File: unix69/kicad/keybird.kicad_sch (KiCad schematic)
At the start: 139 parts, among them J0 Conn_01x23, SW00 SW_Push, SW01 SW_Push, SW02 SW_Push, SW03 SW_Push, SW04 SW_Push, SW05 SW_Push, SW06 SW_Push, SW07 SW_Push, SW10 SW_Push, SW11 SW_Push, SW12 SW_Push, SW13 SW_Push, SW14 SW_Push, SW15 SW_Push, SW16 SW_Push, SW17 SW_Push, SW20 SW_Push, SW21 SW_Push, SW22 SW_Push, SW23 SW_Push, SW24 SW_Push, SW25 SW_Push, SW26 SW_Push, SW27 SW_Push, SW30 SW_Push, SW31 SW_Push, SW32 SW_Push, SW33 SW_Push, SW34 SW_Push, SW35 SW_Push, SW36 SW_Push, SW40 SW_Push, SW41 SW_Push, SW42 SW_Push, SW43 SW_Push, SW44 SW_Push, SW45 SW_Push, SW47 SW_Push, SW50 SW_Push, SW51 SW_Push, SW52 SW_Push, SW53 SW_Push, SW54 SW_Push, SW55 SW_Push, SW56 SW_Push, SW57 SW_Push, SW60 SW_Push, SW61 SW_Push, SW62 SW_Push, SW63 SW_Push, SW64 SW_Push, SW65 SW_Push, SW66 SW_Push, SW67 SW_Push, SW70 SW_Push, SW71 SW_Push, SW72 SW_Push, SW73 SW_Push, SW74 SW_Push, SW75 SW_Push, SW76 SW_Push, SW77 SW_Push, SW80 SW_Push, SW81 SW_Push, SW83 SW_Push, SW84 SW_Push, SW85 SW_Push, SW86 SW_Push, SW87 SW_Push

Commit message: preen annotations and centre rp2040
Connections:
- no-connect marks 80 -> 76
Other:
- note added: "columns on bottom of board"
- note added: "rows on top of board"
- note added: "to Waveshare RP2040-Tiny"
- note removed: "COLUMNS ON BOTTOM OF BOARD"
- note removed: "ROWS ON TOP OF BOARD"
- note removed: "TO GP0"
- note removed: "TO GP1"
- note removed: "TO GP10"
- note removed: "TO GP11"
- note removed: "TO GP12"
- note removed: "TO GP13"
- note removed: "TO GP2"
- note removed: "TO GP26"
- note removed: "TO GP27"
- note removed: "TO GP28"
- note removed: "TO GP29"
- note removed: "TO GP3"
- note removed: "TO GP4"
- note removed: "TO GP5"
- note removed: "TO GP6"
- note removed: "TO GP7"
- note removed: "TO GP8"
- moved on the sheet: J0

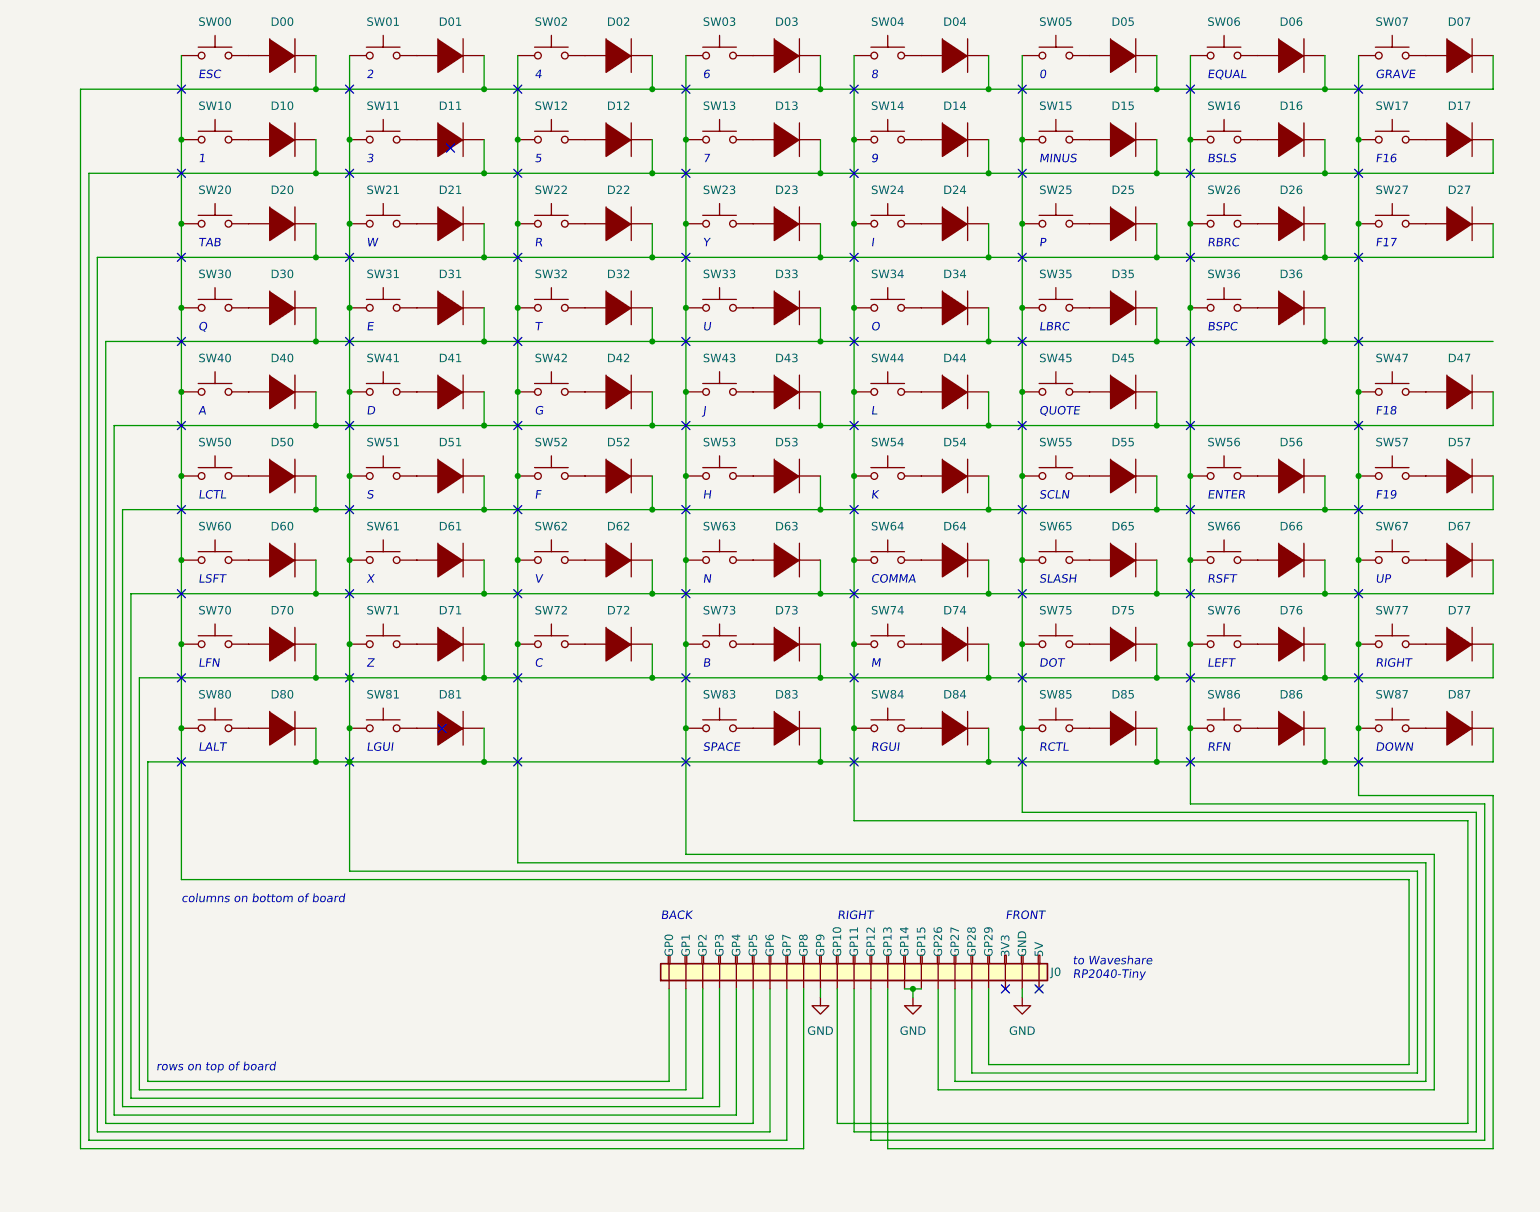
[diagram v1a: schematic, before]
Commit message: use net labels instead of long wires
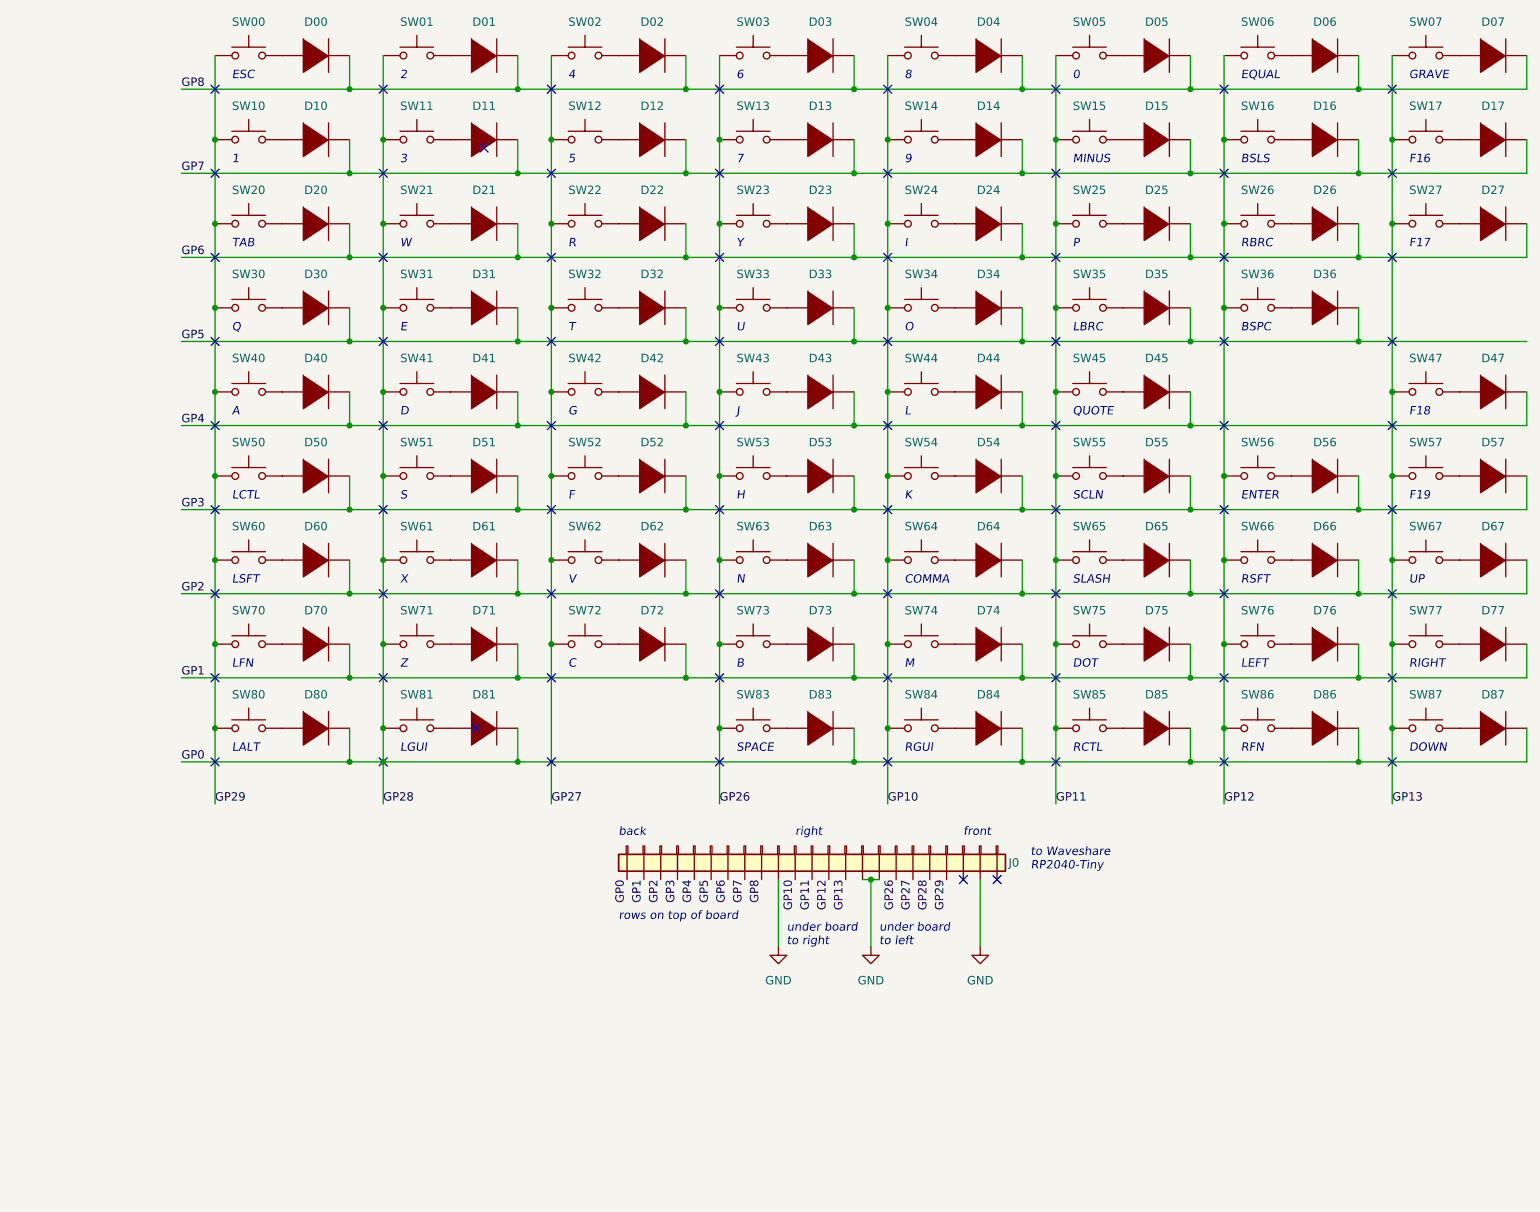
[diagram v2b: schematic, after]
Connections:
- net GP0: now reaches D80.2 (A), D81.2 (A), D83.2 (A), D84.2 (A), D85.2 (A), D86.2 (A), D87.2 (A), J0.1 (GP0), J0.19 (GP28), SW01.1, SW11.1, SW21.1, SW31.1, SW41.1, SW51.1, SW61.1, SW71.1, SW81.1
- net GP0: no longer D70.2 (A), D71.2 (A), D72.2 (A), D73.2 (A), D74.2 (A), D75.2 (A), D76.2 (A), D77.2 (A), J0.2 (GP1)
- net GP10: now reaches J0.11 (GP10), SW04.1, SW14.1, SW24.1, SW34.1, SW44.1, SW54.1, SW64.1, SW74.1, SW84.1
- net GP3: now reaches D50.2 (A), D51.2 (A), D52.2 (A), D53.2 (A), D54.2 (A), D55.2 (A), D56.2 (A), D57.2 (A), J0.4 (GP3)
- net GP2: now reaches D60.2 (A), D61.2 (A), D62.2 (A), D63.2 (A), D64.2 (A), D65.2 (A), D66.2 (A), D67.2 (A), J0.3 (GP2)
- net GP12: now reaches J0.13 (GP12), SW06.1, SW16.1, SW26.1, SW36.1, SW56.1, SW66.1, SW76.1, SW86.1
- net GP26: now reaches J0.17 (GP26), SW03.1, SW13.1, SW23.1, SW33.1, SW43.1, SW53.1, SW63.1, SW73.1, SW83.1
- net GP4: now reaches D40.2 (A), D41.2 (A), D42.2 (A), D43.2 (A), D44.2 (A), D45.2 (A), D47.2 (A), J0.5 (GP4)
- net GP29: now reaches J0.20 (GP29), SW00.1, SW10.1, SW20.1, SW30.1, SW40.1, SW50.1, SW60.1, SW70.1, SW80.1
- net GP27: now reaches J0.18 (GP27), SW02.1, SW12.1, SW22.1, SW32.1, SW42.1, SW52.1, SW62.1, SW72.1
- net GP13: now reaches J0.14 (GP13), SW07.1, SW17.1, SW27.1, SW47.1, SW57.1, SW67.1, SW77.1, SW87.1
- net GP5: now reaches D30.2 (A), D31.2 (A), D32.2 (A), D33.2 (A), D34.2 (A), D35.2 (A), D36.2 (A), J0.6 (GP5)
- net GP11: now reaches J0.12 (GP11), SW05.1, SW15.1, SW25.1, SW35.1, SW45.1, SW55.1, SW65.1, SW75.1, SW85.1
- net GP6: now reaches D20.2 (A), D21.2 (A), D22.2 (A), D23.2 (A), D24.2 (A), D25.2 (A), D26.2 (A), D27.2 (A), J0.7 (GP6)
- net GP8: now reaches D00.2 (A), D01.2 (A), D02.2 (A), D03.2 (A), D04.2 (A), D05.2 (A), D06.2 (A), D07.2 (A), J0.9 (GP8)
- net GP7: now reaches D10.2 (A), D11.2 (A), D12.2 (A), D13.2 (A), D14.2 (A), D15.2 (A), D16.2 (A), D17.2 (A), J0.8 (GP7)
- new net GP1: D70.2 (A), D71.2 (A), D72.2 (A), D73.2 (A), D74.2 (A), D75.2 (A), D76.2 (A), D77.2 (A), J0.2 (GP1)
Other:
- note added: "back"
- note added: "front"
- note added: "right"
- note added: "under board to left"
- note added: "under board to right"
- note removed: "BACK"
- note removed: "FRONT"
- note removed: "columns on bottom of board"
- moved on the sheet: D00, D01, D02, D03, D04, D05, D06, D07, D10, D11, D12, D13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

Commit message: use a proper symbol for the RP20540
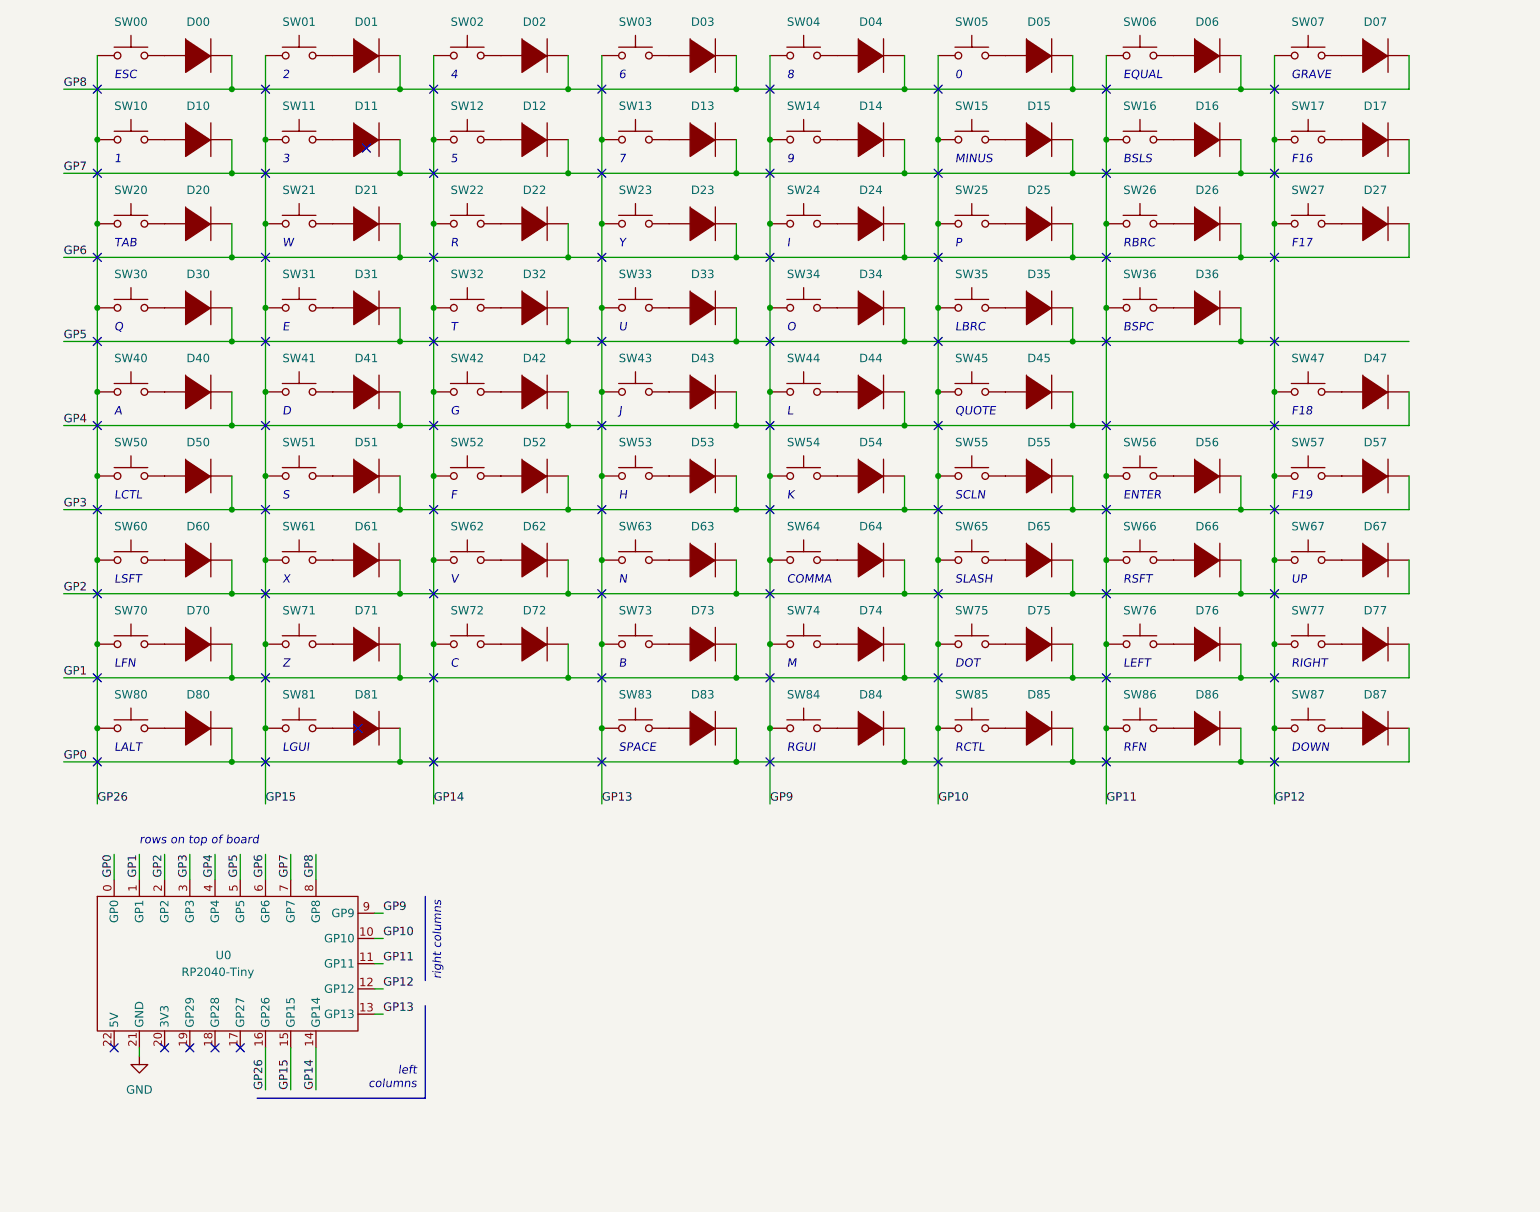
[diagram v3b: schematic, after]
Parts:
- removed J0: Conn_01x23, symbol Connector_Generic:Conn_01x23
- added U0: RP2040-Tiny, Module:RP2040-Tiny, symbol MCU_Module:RP2040-Tiny
- SW00, SW01, SW02, SW03, SW04, SW05, SW06, SW07, SW10, SW11, SW12, SW13, SW14, SW15, SW16, SW17, SW20, SW21, SW22, SW23, SW24, SW25, SW26, SW27, SW30, SW31, SW32, SW33, SW34, SW35, SW36, SW40, SW41, SW42, SW43, SW44, SW45, SW47, SW50, SW51, SW52, SW53, SW54, SW55, SW56, SW57, SW60, SW61, SW62, SW63, SW64, SW65, SW66, SW67, SW70, SW71, SW72, SW73, SW74, SW75, SW76, SW77, SW80, SW81, SW83, SW84, SW85, SW86, SW87: footprint SW_Cherry_MX_1.00u_PCB -> Button_Switch_Keyboard:SW_Cherry_MX_1.00u_PCB
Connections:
- net GP29 is gone; now on net GP26: SW00.1, SW10.1, SW20.1, SW30.1, SW40.1, SW50.1, SW60.1, SW70.1, SW80.1
- net GND: now also U0.21 (GND)
- net GP0: now also U0.0 (GP0); no longer SW01.1, SW11.1, SW21.1, SW31.1, SW41.1, SW51.1, SW61.1, SW71.1, SW81.1
- net GP1: now also U0.1 (GP1)
- net GP10: now also SW05.1, SW15.1, SW25.1, SW35.1, SW45.1, SW55.1, SW65.1, SW75.1, SW85.1, U0.10 (GP10); no longer SW04.1, SW14.1, SW24.1, SW34.1, SW44.1, SW54.1, SW64.1, SW74.1, SW84.1
- net GP11: now also SW06.1, SW16.1, SW26.1, SW36.1, SW56.1, SW66.1, SW76.1, SW86.1, U0.11 (GP11); no longer SW05.1, SW15.1, SW25.1, SW35.1, SW45.1, SW55.1, SW65.1, SW75.1, SW85.1
- net GP12: now also SW07.1, SW17.1, SW27.1, SW47.1, SW57.1, SW67.1, SW77.1, SW87.1, U0.12 (GP12); no longer SW06.1, SW16.1, SW26.1, SW36.1, SW56.1, SW66.1, SW76.1, SW86.1
- net GP13: now also SW03.1, SW13.1, SW23.1, SW33.1, SW43.1, SW53.1, SW63.1, SW73.1, SW83.1, U0.13 (GP13); no longer SW07.1, SW17.1, SW27.1, SW47.1, SW57.1, SW67.1, SW77.1, SW87.1
- net GP2: now also U0.2 (GP2)
- net GP26: now also U0.16 (GP26); no longer SW03.1, SW13.1, SW23.1, SW33.1, SW43.1, SW53.1, SW63.1, SW73.1, SW83.1
- net GP3: now also U0.3 (GP3)
- net GP4: now also U0.4 (GP4)
- net GP5: now also U0.5 (GP5)
- net GP6: now also U0.6 (GP6)
- net GP7: now also U0.7 (GP7)
- net GP8: now also U0.8 (GP8)
- net GP27 renamed GP14
- net GP14: now also U0.14 (GP14)
- new net GP15: SW01.1, SW11.1, SW21.1, SW31.1, SW41.1, SW51.1, SW61.1, SW71.1, SW81.1, U0.15 (GP15)
- new net GP9: SW04.1, SW14.1, SW24.1, SW34.1, SW44.1, SW54.1, SW64.1, SW74.1, SW84.1, U0.9 (GP9)
- no-connect marks 76 -> 79
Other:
- note added: "left columns"
- note added: "right columns"
- note removed: "back"
- note removed: "front"
- note removed: "right"
- note removed: "to Waveshare RP2040-Tiny"
- note removed: "under board to left"
- note removed: "under board to right"
- moved on the sheet: D00, D01, D02, D03, D04, D05, D06, D07, D10, D11, D12, D13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

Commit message: much work on the pcb
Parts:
- SW00, SW01, SW02, SW03, SW04, SW05, SW06, SW07, SW10, SW11, SW12, SW13, SW14, SW15, SW16, SW17, SW21, SW22, SW23, SW24, SW25, SW26, SW27, SW30, SW31, SW32, SW33, SW34, SW35, SW40, SW41, SW42, SW43, SW44, SW45, SW47, SW51, SW52, SW53, SW54, SW55, SW57, SW61, SW62, SW63, SW64, SW65, SW67, SW71, SW72, SW73, SW74, SW75, SW76, SW77, SW84, SW85, SW86, SW87: footprint Button_Switch_Keyboard:SW_Cherry_MX_1.00u_PCB -> Switch_Keyboard_Hotswap_Kailh:SW_Hotswap_Kailh_MX_1.00u
- SW20, SW36: footprint Button_Switch_Keyboard:SW_Cherry_MX_1.00u_PCB -> Switch_Keyboard_Hotswap_Kailh:SW_Hotswap_Kailh_MX_1.50u
- SW50, SW66: footprint Button_Switch_Keyboard:SW_Cherry_MX_1.00u_PCB -> Switch_Keyboard_Hotswap_Kailh:SW_Hotswap_Kailh_MX_1.75u
- SW56, SW60: footprint Button_Switch_Keyboard:SW_Cherry_MX_1.00u_PCB -> Switch_Keyboard_Hotswap_Kailh:SW_Hotswap_Kailh_MX_2.25u
- SW70, SW80, SW81: footprint Button_Switch_Keyboard:SW_Cherry_MX_1.00u_PCB -> Switch_Keyboard_Hotswap_Kailh:SW_Hotswap_Kailh_MX_1.25u
- SW83: footprint Button_Switch_Keyboard:SW_Cherry_MX_1.00u_PCB -> Switch_Keyboard_Hotswap_Kailh:SW_Hotswap_Kailh_MX_6.25u
